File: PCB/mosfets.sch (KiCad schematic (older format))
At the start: 16 parts

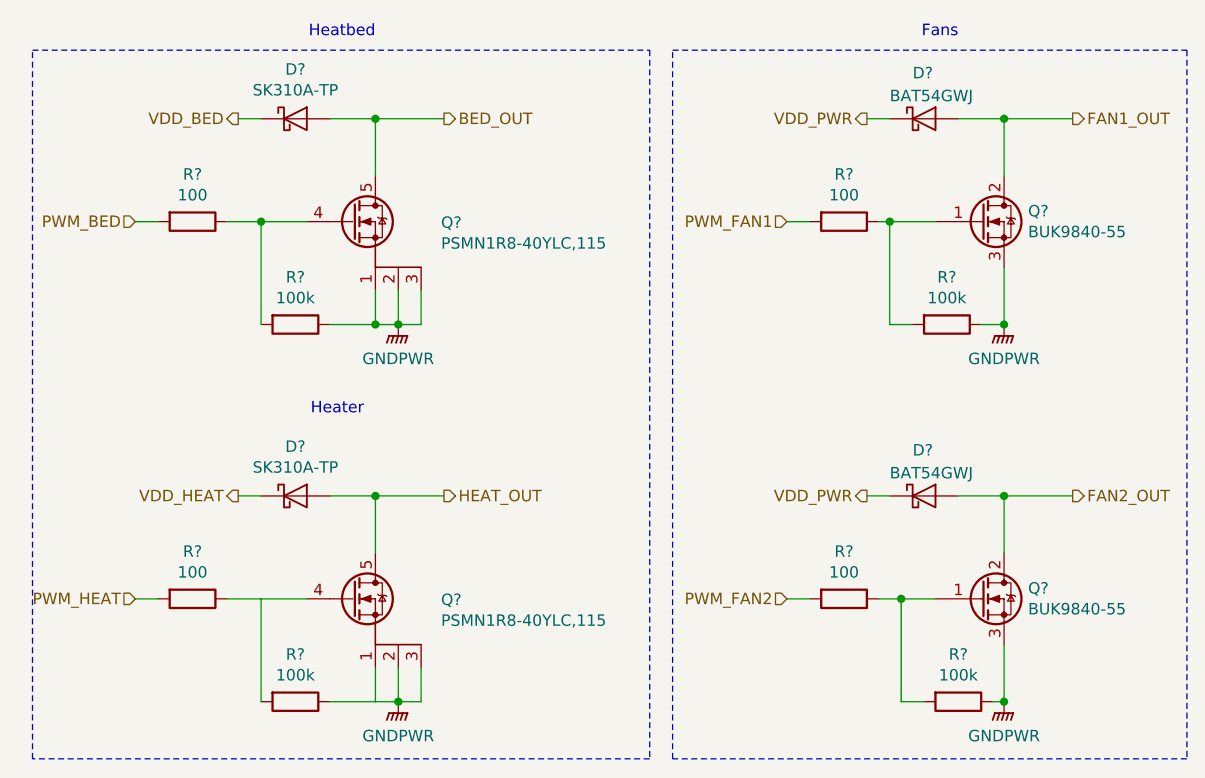
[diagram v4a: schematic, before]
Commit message: Fixed bugs found with ERC.
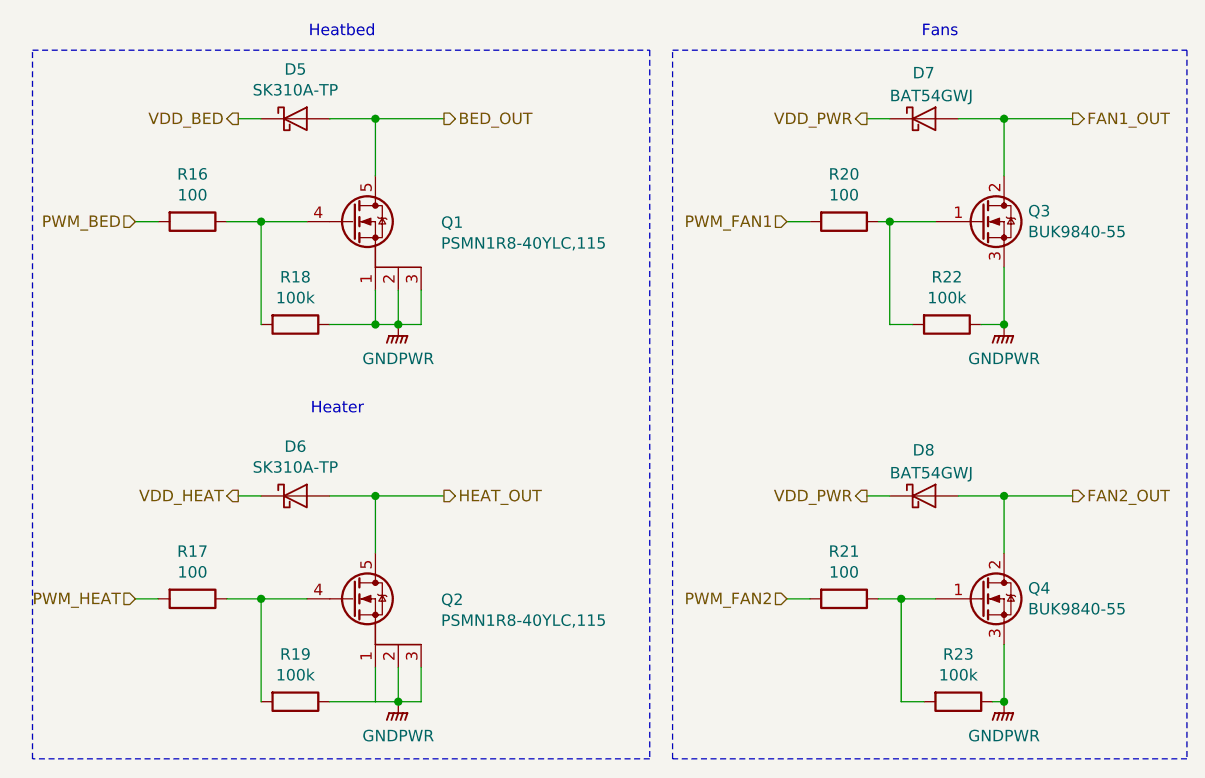
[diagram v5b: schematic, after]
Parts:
- gave numbers to parts that had none: 16
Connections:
- net at R19.2: now also Q2.4 (G), R17.1
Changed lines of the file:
@@
 Fans
 $Comp
-L power:GNDPWR #PWR?
+L power:GNDPWR #PWR048
 U 1 1 5B1A30B2
 P 2200 1850
-F 0 "#PWR?" H 2200 1650 50  0001 C CNN
+F 0 "#PWR048" H 2200 1650 50  0001 C CNN
 F 1 "GNDPWR" H 2200 1700 50  0000 C CNN
 F 2 "" H 2200 1800 50  0001 C CNN
@@
 VDD_BED
 $Comp
-L Device:D_Schottky D?
+L Device:D_Schottky D5
 U 1 1 5B1A3271
 P 1750 950
-F 0 "D?" H 1750 1166 50  0000 C CNN
+F 0 "D5" H 1750 1166 50  0000 C CNN
 F 1 "SK310A-TP" H 1750 1075 50  0000 C CNN
 F 2 "Diode_SMD:D_SMA" H 1750 950 50  0001 C CNN
@@
 	1500 950  1600 950
 $Comp
-L remram-custom:PSMN1R8-40YLC,115 Q?
+L remram-custom:PSMN1R8-40YLC,115 Q1
 U 1 1 5B1A764D
 P 2000 1400
-F 0 "Q?" H 2387 1396 50  0000 L CNN
+F 0 "Q1" H 2387 1396 50  0000 L CNN
 F 1 "PSMN1R8-40YLC,115" H 2387 1305 50  0000 L CNN
 F 2 "Package_TO_SOT_SMD:SOT-669_LFPAK_ThermalVias-1" H 2200 1325 50  0001 L CIN
@@
 PWM_HEAT
 $Comp
-L Device:R R?
+L Device:R R16
 U 1 1 5B1AEA5D
 P 1300 1400
-F 0 "R?" V 1093 1400 50  0000 C CNN
+F 0 "R16" V 1093 1400 50  0000 C CNN
 F 1 "100" V 1184 1400 50  0000 C CNN
 F 2 "Resistor_SMD:R_0603_1608Metric" V 1230 1400 50  0001 C CNN
@@
 	2100 1200 2100 950
 $Comp
-L power:GNDPWR #PWR?
+L power:GNDPWR #PWR049
 U 1 1 5B1B03AE
 P 2200 3500
-F 0 "#PWR?" H 2200 3300 50  0001 C CNN
+F 0 "#PWR049" H 2200 3300 50  0001 C CNN
 F 1 "GNDPWR" H 2200 3350 50  0000 C CNN
 F 2 "" H 2200 3450 50  0001 C CNN
@@
 VDD_HEAT
 $Comp
-L Device:D_Schottky D?
+L Device:D_Schottky D6
 U 1 1 5B1B03B6
 P 1750 2600
-F 0 "D?" H 1750 2816 50  0000 C CNN
+F 0 "D6" H 1750 2816 50  0000 C CNN
 F 1 "SK310A-TP" H 1750 2725 50  0000 C CNN
 F 2 "Diode_SMD:D_SMA" H 1750 2600 50  0001 C CNN
@@
 	1500 2600 1600 2600
 $Comp
-L remram-custom:PSMN1R8-40YLC,115 Q?
+L remram-custom:PSMN1R8-40YLC,115 Q2
 U 1 1 5B1B03C5
 P 2000 3050
-F 0 "Q?" H 2387 3046 50  0000 L CNN
+F 0 "Q2" H 2387 3046 50  0000 L CNN
 F 1 "PSMN1R8-40YLC,115" H 2387 2955 50  0000 L CNN
 F 2 "Package_TO_SOT_SMD:SOT-669_LFPAK_ThermalVias-1" H 2200 2975 50  0001 L CIN
@@
 	2100 3500 2100 3350
 $Comp
-L Device:R R?
+L Device:R R17
 U 1 1 5B1B03DE
 P 1300 3050
-F 0 "R?" V 1093 3050 50  0000 C CNN
+F 0 "R17" V 1093 3050 50  0000 C CNN
 F 1 "100" V 1184 3050 50  0000 C CNN
 F 2 "Resistor_SMD:R_0603_1608Metric" V 1230 3050 50  0001 C CNN
@@
 Connection ~ 2100 2600
 $Comp
-L remram-custom:BUK9840-55 Q?
+L remram-custom:BUK9840-55 Q3
 U 1 1 5B1FB146
 P 4750 1400
-F 0 "Q?" H 4955 1446 50  0000 L CNN
+F 0 "Q3" H 4955 1446 50  0000 L CNN
 F 1 "BUK9840-55" H 4955 1355 50  0000 L CNN
 F 2 "Package_TO_SOT_SMD:SOT-223-3_TabPin2" H 4950 1325 50  0001 L CIN
@@
 $EndComp
 $Comp
-L Device:R R?
+L Device:R R20
 U 1 1 5B1FB287
 P 4150 1400
-F 0 "R?" V 3943 1400 50  0000 C CNN
+F 0 "R20" V 3943 1400 50  0000 C CNN
 F 1 "100" V 4034 1400 50  0000 C CNN
 F 2 "Resistor_SMD:R_0603_1608Metric" V 4080 1400 50  0001 C CNN
@@
 	3900 1400 4000 1400
 $Comp
-L power:GNDPWR #PWR?
+L power:GNDPWR #PWR050
 U 1 1 5B1FD93D
 P 4850 1850
-F 0 "#PWR?" H 4850 1650 50  0001 C CNN
+F 0 "#PWR050" H 4850 1650 50  0001 C CNN
 F 1 "GNDPWR" H 4850 1700 50  0000 C CNN
 F 2 "" H 4850 1800 50  0001 C CNN
@@
 	4850 1600 4850 1850
 $Comp
-L remram-custom:BUK9840-55 Q?
+L remram-custom:BUK9840-55 Q4
 U 1 1 5B2008C9
 P 4750 3050
-F 0 "Q?" H 4955 3096 50  0000 L CNN
+F 0 "Q4" H 4955 3096 50  0000 L CNN
 F 1 "BUK9840-55" H 4955 3005 50  0000 L CNN
 F 2 "Package_TO_SOT_SMD:SOT-223-3_TabPin2" H 4950 2975 50  0001 L CIN
@@
 $EndComp
 $Comp
-L Device:R R?
+L Device:R R21
 U 1 1 5B2008D0
 P 4150 3050
-F 0 "R?" V 3943 3050 50  0000 C CNN
+F 0 "R21" V 3943 3050 50  0000 C CNN
 F 1 "100" V 4034 3050 50  0000 C CNN
 F 2 "Resistor_SMD:R_0603_1608Metric" V 4080 3050 50  0001 C CNN
@@
 	3900 3050 4000 3050
 $Comp
-L power:GNDPWR #PWR?
+L power:GNDPWR #PWR051
 U 1 1 5B2008E5
 P 4850 3500
-F 0 "#PWR?" H 4850 3300 50  0001 C CNN
+F 0 "#PWR051" H 4850 3300 50  0001 C CNN
 F 1 "GNDPWR" H 4850 3350 50  0000 C CNN
 F 2 "" H 4850 3450 50  0001 C CNN
@@
 	1450 1400 1600 1400
 Wire Wire Line
-	1450 3050 1800 3050
-$Comp
-L Device:R R?
+	1450 3050 1600 3050
+$Comp
+L Device:R R18
 U 1 1 5AF82135
 P 1750 1850
-F 0 "R?" V 1543 1850 50  0000 C CNN
+F 0 "R18" V 1543 1850 50  0000 C CNN
 F 1 "100k" V 1634 1850 50  0000 C CNN
 F 2 "Resistor_SMD:R_0603_1608Metric" V 1680 1850 50  0001 C CNN
@@
 	1600 1400 1800 1400
 $Comp
-L Device:R R?
+L Device:R R19
 U 1 1 5AF8339E
 P 1750 3500
-F 0 "R?" V 1543 3500 50  0000 C CNN
+F 0 "R19" V 1543 3500 50  0000 C CNN
 F 1 "100k" V 1634 3500 50  0000 C CNN
 F 2 "Resistor_SMD:R_0603_1608Metric" V 1680 3500 50  0001 C CNN
@@
 Wire Wire Line
 	2100 3500 1900 3500
-Wire Wire Line
-	1600 3500 1600 3050
-$Comp
-L Device:R R?
+$Comp
+L Device:R R22
 U 1 1 5AF83BB4
 P 4600 1850
-F 0 "R?" V 4393 1850 50  0000 C CNN
+F 0 "R22" V 4393 1850 50  0000 C CNN
 F 1 "100k" V 4484 1850 50  0000 C CNN
 F 2 "Resistor_SMD:R_0603_1608Metric" V 4530 1850 50  0001 C CNN
@@
 Connection ~ 4350 1400
 $Comp
-L Device:R R?
+L Device:R R23
 U 1 1 5AF880C0
 P 4650 3500
-F 0 "R?" V 4443 3500 50  0000 C CNN
+F 0 "R23" V 4443 3500 50  0000 C CNN
 F 1 "100k" V 4534 3500 50  0000 C CNN
 F 2 "Resistor_SMD:R_0603_1608Metric" V 4580 3500 50  0001 C CNN
@@
 Connection ~ 4850 3500
 $Comp
-L Device:D_Schottky D?
+L Device:D_Schottky D7
 U 1 1 5AFB8598
 P 4500 950
-F 0 "D?" H 4450 1150 50  0000 L CNN
+F 0 "D7" H 4450 1150 50  0000 L CNN
 F 1 "BAT54GWJ" H 4350 1050 50  0000 L CNN
 F 2 "Diode_SMD:D_SOD-123" H 4500 950 50  0001 C CNN
@@
 $EndComp
 $Comp
-L Device:D_Schottky D?
+L Device:D_Schottky D8
 U 1 1 5AFBAFD7
 P 4500 2600
-F 0 "D?" H 4450 2800 50  0000 L CNN
+F 0 "D8" H 4450 2800 50  0000 L CNN
 F 1 "BAT54GWJ" H 4350 2700 50  0000 L CNN
 F 2 "Diode_SMD:D_SOD-123" H 4500 2600 50  0001 C CNN
@@
 	1    0    0    -1
 $EndComp
+Wire Wire Line
+	1600 3500 1600 3050
+Connection ~ 1600 3050
+Wire Wire Line
+	1600 3050 1800 3050
 $EndSCHEMATC

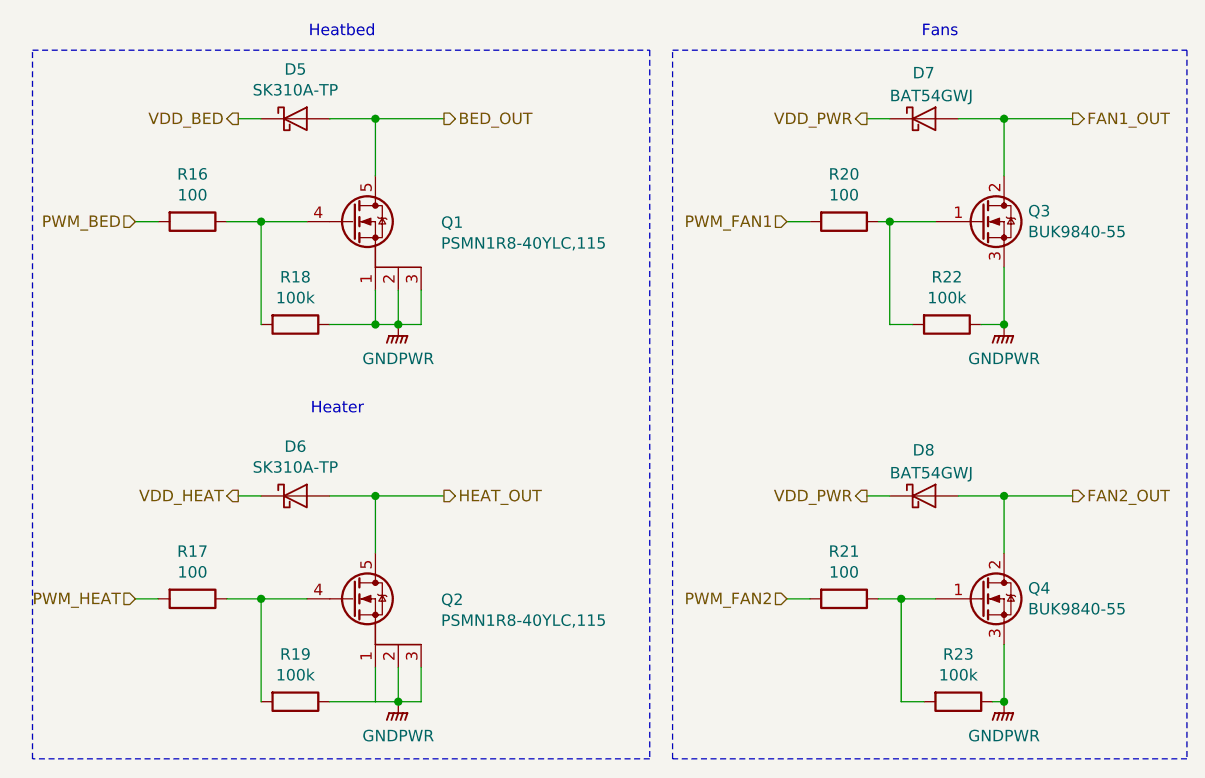
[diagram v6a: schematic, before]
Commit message: Saving work in progress.
Every component now has a 3D mode.
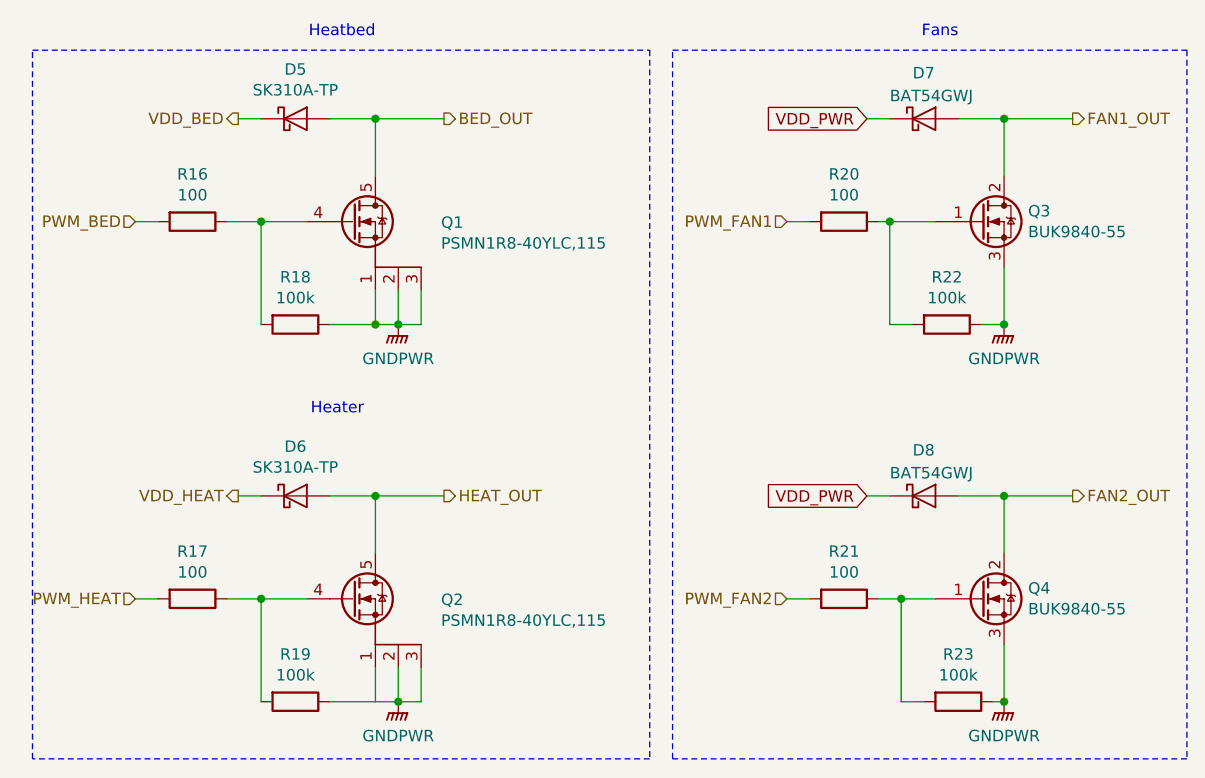
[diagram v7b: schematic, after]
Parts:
- Q1, Q2: footprint Package_TO_SOT_SMD:SOT-669_LFPAK_ThermalVias-1 -> Package_TO_SOT_SMD:SOT-669_LFPAK_ThermalVias-2
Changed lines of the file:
@@
 F 0 "Q1" H 2387 1396 50  0000 L CNN
 F 1 "PSMN1R8-40YLC,115" H 2387 1305 50  0000 L CNN
-F 2 "Package_TO_SOT_SMD:SOT-669_LFPAK_ThermalVias-1" H 2200 1325 50  0001 L CIN
+F 2 "Package_TO_SOT_SMD:SOT-669_LFPAK_ThermalVias-2" H 2200 1325 50  0001 L CIN
 F 3 "https://assets.nexperia.com/documents/data-sheet/PSMN1R8-40YLC.pdf" V 2000 1400 50  0001 L CNN
 	1    2000 1400
@@
 F 0 "Q2" H 2387 3046 50  0000 L CNN
 F 1 "PSMN1R8-40YLC,115" H 2387 2955 50  0000 L CNN
-F 2 "Package_TO_SOT_SMD:SOT-669_LFPAK_ThermalVias-1" H 2200 2975 50  0001 L CIN
+F 2 "Package_TO_SOT_SMD:SOT-669_LFPAK_ThermalVias-2" H 2200 2975 50  0001 L CIN
 F 3 "https://assets.nexperia.com/documents/data-sheet/PSMN1R8-40YLC.pdf" V 2000 3050 50  0001 L CNN
 	1    2000 3050
@@
 Text HLabel 5150 950  2    50   Output ~ 0
 FAN1_OUT
-Text HLabel 4250 950  0    50   Output ~ 0
-VDD_PWR
 Wire Wire Line
 	4250 950  4350 950
@@
 Text HLabel 5150 2600 2    50   Output ~ 0
 FAN2_OUT
-Text HLabel 4250 2600 0    50   Output ~ 0
-VDD_PWR
 Wire Wire Line
 	4250 2600 4350 2600
@@
 Wire Wire Line
 	1600 3050 1800 3050
+Text GLabel 4250 950  0    50   Input ~ 0
+VDD_PWR
+Text GLabel 4250 2600 0    50   Input ~ 0
+VDD_PWR
 $EndSCHEMATC

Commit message: Removed logic level converter. Changed LDO.
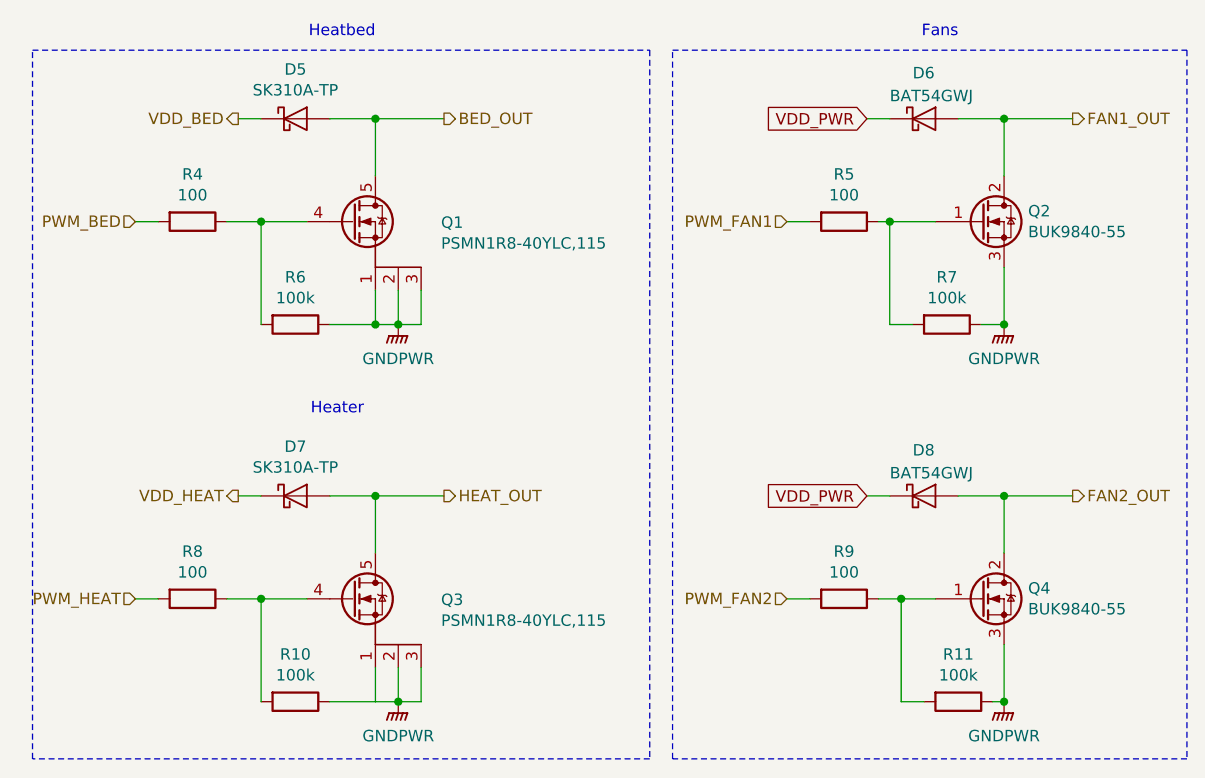
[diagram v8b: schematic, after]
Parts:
- renumbered D7 to D6, D6 to D7, Q3 to Q2, Q2 to Q3, R19 to R10, R23 to R11, R16 to R4, R20 to R5, R18 to R6, R22 to R7, R17 to R8, R21 to R9
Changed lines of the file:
@@
 $Descr A4 11693 8268
 encoding utf-8
-Sheet 4 9
+Sheet 3 9
 Title "MOSFET"
 Date ""
@@
 Fans
 $Comp
-L power:GNDPWR #PWR048
+L power:GNDPWR #PWR026
 U 1 1 5B1A30B2
 P 2200 1850
-F 0 "#PWR048" H 2200 1650 50  0001 C CNN
+F 0 "#PWR026" H 2200 1650 50  0001 C CNN
 F 1 "GNDPWR" H 2200 1700 50  0000 C CNN
 F 2 "" H 2200 1800 50  0001 C CNN
@@
 PWM_HEAT
 $Comp
-L Device:R R16
+L Device:R R4
 U 1 1 5B1AEA5D
 P 1300 1400
-F 0 "R16" V 1093 1400 50  0000 C CNN
+F 0 "R4" V 1093 1400 50  0000 C CNN
 F 1 "100" V 1184 1400 50  0000 C CNN
 F 2 "Resistor_SMD:R_0603_1608Metric" V 1230 1400 50  0001 C CNN
@@
 	2100 1200 2100 950
 $Comp
-L power:GNDPWR #PWR049
+L power:GNDPWR #PWR028
 U 1 1 5B1B03AE
 P 2200 3500
-F 0 "#PWR049" H 2200 3300 50  0001 C CNN
+F 0 "#PWR028" H 2200 3300 50  0001 C CNN
 F 1 "GNDPWR" H 2200 3350 50  0000 C CNN
 F 2 "" H 2200 3450 50  0001 C CNN
@@
 VDD_HEAT
 $Comp
-L Device:D_Schottky D6
+L Device:D_Schottky D7
 U 1 1 5B1B03B6
 P 1750 2600
-F 0 "D6" H 1750 2816 50  0000 C CNN
+F 0 "D7" H 1750 2816 50  0000 C CNN
 F 1 "SK310A-TP" H 1750 2725 50  0000 C CNN
 F 2 "Diode_SMD:D_SMA" H 1750 2600 50  0001 C CNN
@@
 	1500 2600 1600 2600
 $Comp
-L remram-custom:PSMN1R8-40YLC,115 Q2
+L remram-custom:PSMN1R8-40YLC,115 Q3
 U 1 1 5B1B03C5
 P 2000 3050
-F 0 "Q2" H 2387 3046 50  0000 L CNN
+F 0 "Q3" H 2387 3046 50  0000 L CNN
 F 1 "PSMN1R8-40YLC,115" H 2387 2955 50  0000 L CNN
 F 2 "Package_TO_SOT_SMD:SOT-669_LFPAK_ThermalVias-2" H 2200 2975 50  0001 L CIN
@@
 	2100 3500 2100 3350
 $Comp
-L Device:R R17
+L Device:R R8
 U 1 1 5B1B03DE
 P 1300 3050
-F 0 "R17" V 1093 3050 50  0000 C CNN
+F 0 "R8" V 1093 3050 50  0000 C CNN
 F 1 "100" V 1184 3050 50  0000 C CNN
 F 2 "Resistor_SMD:R_0603_1608Metric" V 1230 3050 50  0001 C CNN
@@
 Connection ~ 2100 2600
 $Comp
-L remram-custom:BUK9840-55 Q3
+L remram-custom:BUK9840-55 Q2
 U 1 1 5B1FB146
 P 4750 1400
-F 0 "Q3" H 4955 1446 50  0000 L CNN
+F 0 "Q2" H 4955 1446 50  0000 L CNN
 F 1 "BUK9840-55" H 4955 1355 50  0000 L CNN
 F 2 "Package_TO_SOT_SMD:SOT-223-3_TabPin2" H 4950 1325 50  0001 L CIN
@@
 $EndComp
 $Comp
-L Device:R R20
+L Device:R R5
 U 1 1 5B1FB287
 P 4150 1400
-F 0 "R20" V 3943 1400 50  0000 C CNN
+F 0 "R5" V 3943 1400 50  0000 C CNN
 F 1 "100" V 4034 1400 50  0000 C CNN
 F 2 "Resistor_SMD:R_0603_1608Metric" V 4080 1400 50  0001 C CNN
@@
 	3900 1400 4000 1400
 $Comp
-L power:GNDPWR #PWR050
+L power:GNDPWR #PWR027
 U 1 1 5B1FD93D
 P 4850 1850
-F 0 "#PWR050" H 4850 1650 50  0001 C CNN
+F 0 "#PWR027" H 4850 1650 50  0001 C CNN
 F 1 "GNDPWR" H 4850 1700 50  0000 C CNN
 F 2 "" H 4850 1800 50  0001 C CNN
@@
 $EndComp
 $Comp
-L Device:R R21
+L Device:R R9
 U 1 1 5B2008D0
 P 4150 3050
-F 0 "R21" V 3943 3050 50  0000 C CNN
+F 0 "R9" V 3943 3050 50  0000 C CNN
 F 1 "100" V 4034 3050 50  0000 C CNN
 F 2 "Resistor_SMD:R_0603_1608Metric" V 4080 3050 50  0001 C CNN
@@
 	3900 3050 4000 3050
 $Comp
-L power:GNDPWR #PWR051
+L power:GNDPWR #PWR029
 U 1 1 5B2008E5
 P 4850 3500
-F 0 "#PWR051" H 4850 3300 50  0001 C CNN
+F 0 "#PWR029" H 4850 3300 50  0001 C CNN
 F 1 "GNDPWR" H 4850 3350 50  0000 C CNN
 F 2 "" H 4850 3450 50  0001 C CNN
@@
 	1450 3050 1600 3050
 $Comp
-L Device:R R18
+L Device:R R6
 U 1 1 5AF82135
 P 1750 1850
-F 0 "R18" V 1543 1850 50  0000 C CNN
+F 0 "R6" V 1543 1850 50  0000 C CNN
 F 1 "100k" V 1634 1850 50  0000 C CNN
 F 2 "Resistor_SMD:R_0603_1608Metric" V 1680 1850 50  0001 C CNN
@@
 	1600 1400 1800 1400
 $Comp
-L Device:R R19
+L Device:R R10
 U 1 1 5AF8339E
 P 1750 3500
-F 0 "R19" V 1543 3500 50  0000 C CNN
+F 0 "R10" V 1543 3500 50  0000 C CNN
 F 1 "100k" V 1634 3500 50  0000 C CNN
 F 2 "Resistor_SMD:R_0603_1608Metric" V 1680 3500 50  0001 C CNN
@@
 	2100 3500 1900 3500
 $Comp
-L Device:R R22
+L Device:R R7
 U 1 1 5AF83BB4
 P 4600 1850
-F 0 "R22" V 4393 1850 50  0000 C CNN
+F 0 "R7" V 4393 1850 50  0000 C CNN
 F 1 "100k" V 4484 1850 50  0000 C CNN
 F 2 "Resistor_SMD:R_0603_1608Metric" V 4530 1850 50  0001 C CNN
@@
 Connection ~ 4350 1400
 $Comp
-L Device:R R23
+L Device:R R11
 U 1 1 5AF880C0
 P 4650 3500
-F 0 "R23" V 4443 3500 50  0000 C CNN
+F 0 "R11" V 4443 3500 50  0000 C CNN
 F 1 "100k" V 4534 3500 50  0000 C CNN
 F 2 "Resistor_SMD:R_0603_1608Metric" V 4580 3500 50  0001 C CNN
@@
 Connection ~ 4850 3500
 $Comp
-L Device:D_Schottky D7
+L Device:D_Schottky D6
 U 1 1 5AFB8598
 P 4500 950
-F 0 "D7" H 4450 1150 50  0000 L CNN
+F 0 "D6" H 4450 1150 50  0000 L CNN
 F 1 "BAT54GWJ" H 4350 1050 50  0000 L CNN
 F 2 "Diode_SMD:D_SOD-123" H 4500 950 50  0001 C CNN
